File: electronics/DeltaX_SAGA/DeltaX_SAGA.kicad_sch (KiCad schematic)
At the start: 68 parts, among them J1 USB_B_Micro, J10 Motor3_Encoder, J11 Motor1_OUT, J12 Motor2_OUT, J13 Motor3_OUT, J14 TestPt1, J15 TestPt2, J16 TestGND, J18 STLink, J2 Programmer, J3 Servo Signal, J4 Servo Power, J5 Power(6-38V), J6 Thrower Signal, J7 Thrower Power, J8 Motor1_Encoder, J9 Motor2_Encoder, U1 CM1223, U10 DRV8243, U11 DRV8243, U2 NCP164C, U3 STM32G441KB, U4 NCV8730, U5 NCP164C, U6 MAX14930, U7 MAX14930, U8 MAX12930, U9 DRV8243

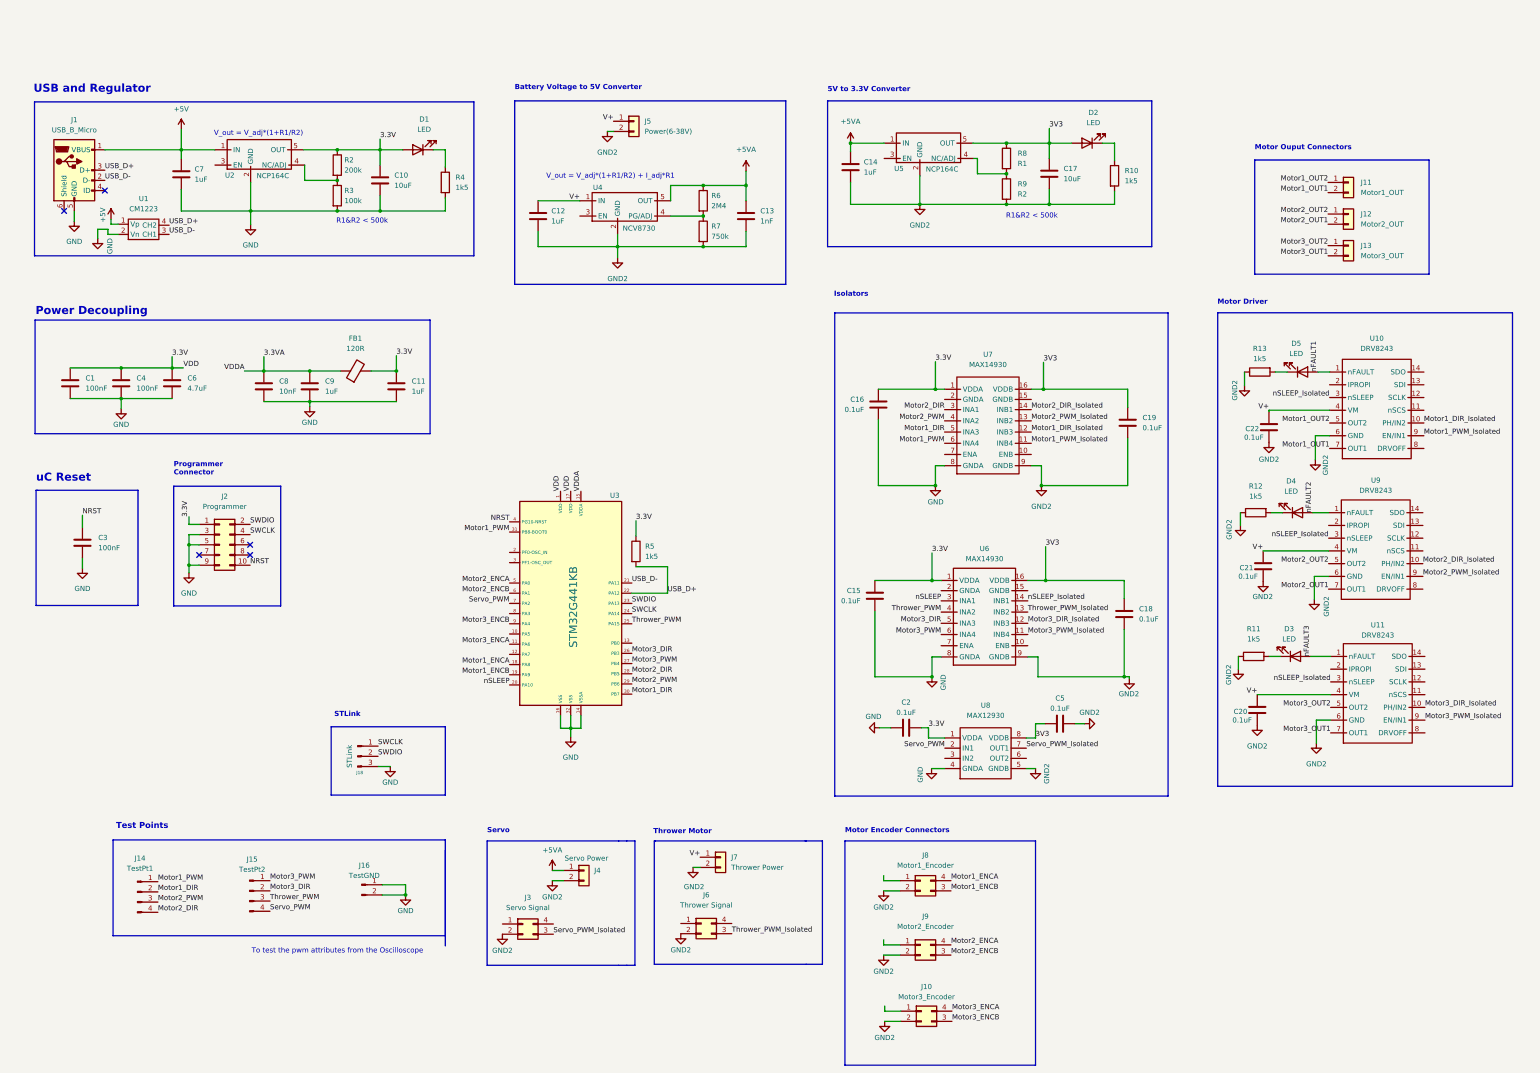
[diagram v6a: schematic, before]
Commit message: Board schematic updated
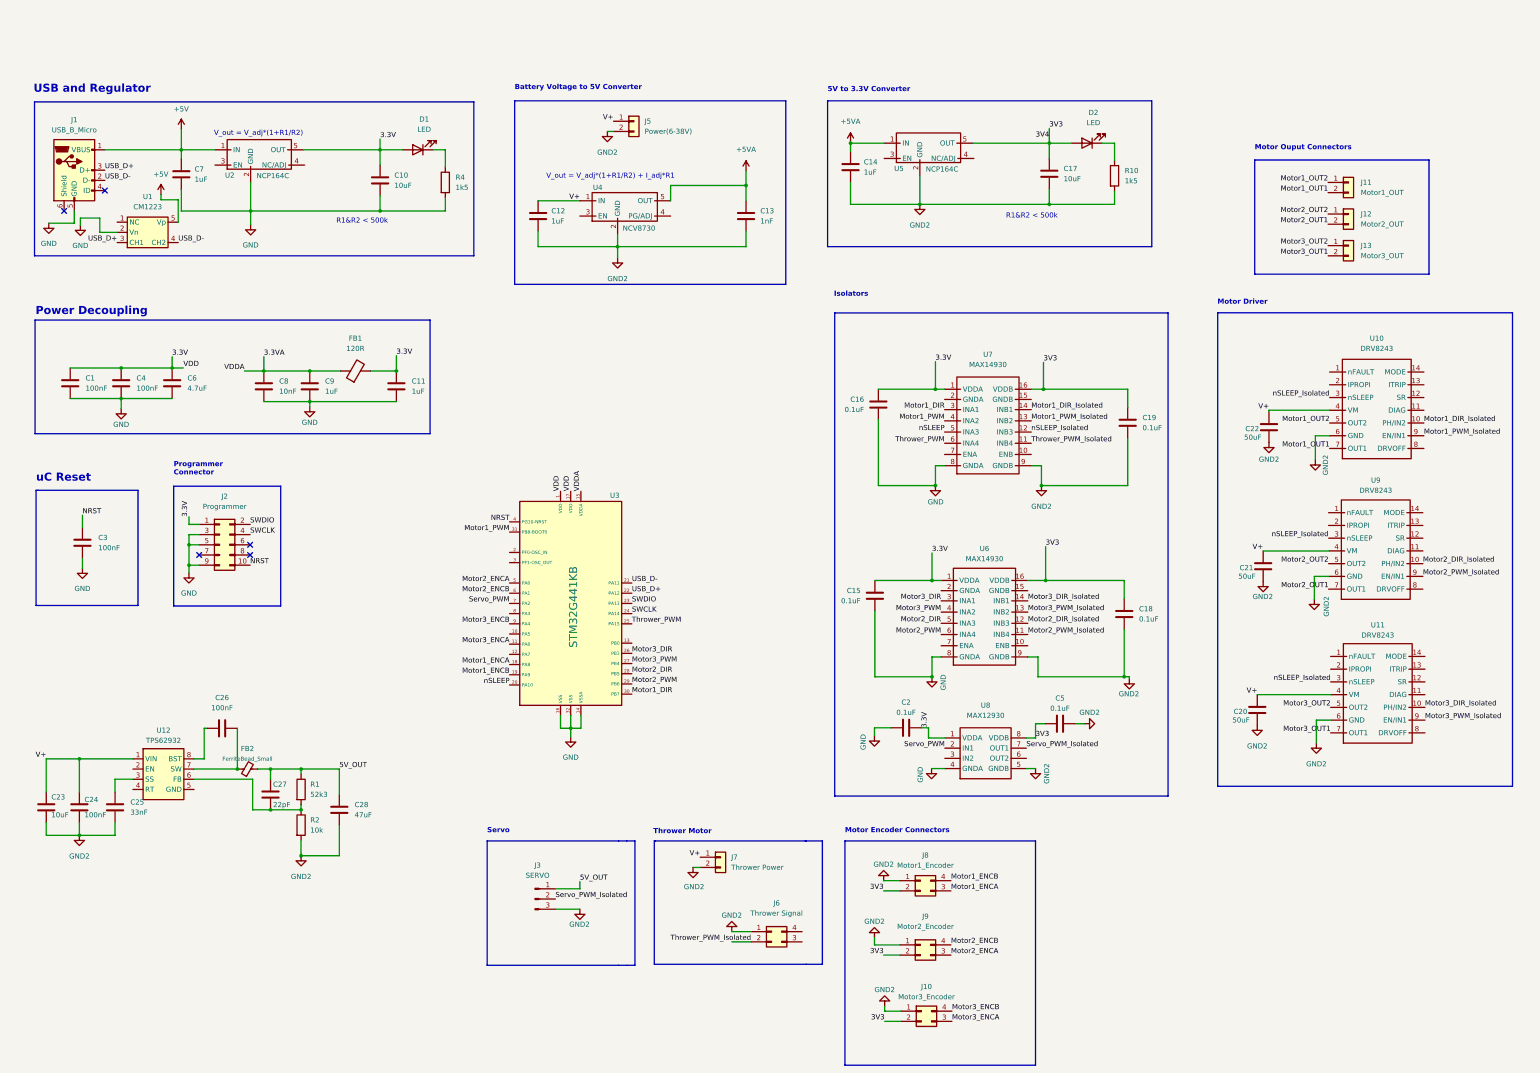
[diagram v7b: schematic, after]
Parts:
- removed D3, D4, D5: LED, LED_SMD:LED_0603_1608Metric, symbol Device:LED
- removed J14: TestPt1, Connector_PinHeader_2.54mm:PinHeader_1x04_P2.54mm_Vertical, symbol Connector:Conn_01x04_Male
- removed J15: TestPt2, Connector_PinHeader_2.54mm:PinHeader_1x04_P2.54mm_Vertical, symbol Connector:Conn_01x04_Male
- removed J16: TestGND, Connector_PinHeader_2.54mm:PinHeader_1x02_P2.54mm_Vertical, symbol Connector:Conn_01x02_Male
- removed J18: STLink, Connector_PinHeader_2.54mm:PinHeader_1x03_P2.54mm_Vertical, symbol Connector:Conn_01x03_Male
- removed J3: Servo Signal, Micro-MaTch215079-4:TE_7-215079-4, symbol Connector_Generic:Conn_02x02_Counter_Clockwise
- removed J4: Servo Power, Connector_PinHeader_2.54mm:PinHeader_1x02_P2.54mm_Vertical_SMD_Pin1Right, symbol Connector_Generic:Conn_01x02
- removed R11, R12, R13, R5: 1k5, Resistor_SMD:R_0402_1005Metric, symbol Device:R
- removed R3: 100k, Resistor_SMD:R_0402_1005Metric, symbol Device:R
- removed R6: 2M4, Resistor_SMD:R_0402_1005Metric, symbol Device:R
- removed R7: 750k, Resistor_SMD:R_0402_1005Metric, symbol Device:R
- removed R8: R1, Resistor_SMD:R_0402_1005Metric, symbol Device:R
- removed R9: R2, Resistor_SMD:R_0402_1005Metric, symbol Device:R
- added C23: 10uF, Capacitor_SMD:C_0603_1608Metric, symbol Device:C
- added C24, C26: 100nF, Capacitor_SMD:C_0603_1608Metric, symbol Device:C
- added C25: 33nF, Capacitor_SMD:C_0603_1608Metric, symbol Device:C
- added C27: 22pF, Capacitor_SMD:C_0603_1608Metric, symbol Device:C
- added C28: 47uF, Capacitor_SMD:C_0603_1608Metric, symbol Device:C
- added FB2: FerriteBead_Small, Inductor_SMD:L_0603_1608Metric, symbol Device:FerriteBead_Small
- added J3: SERVO, Connector_PinHeader_2.54mm:PinHeader_1x03_P2.54mm_Vertical, symbol Connector:Conn_01x03_Male
- added R1: 52k3, Resistor_SMD:R_0603_1608Metric, symbol Device:R
- added U12: TPS62932, TPS62933:TPS62933, symbol TPS62932:TPS62932
- C1, C11, C12, C13, C14, C15, C16, C18, C19, C2, C3, C4, C5, C7, C8, C9: footprint Capacitor_SMD:C_0402_1005Metric -> Capacitor_SMD:C_0603_1608Metric
- C20, C21, C22: value 0.1uF -> 50uF; footprint Capacitor_SMD:C_0402_1005Metric -> Capacitor_SMD:C_0603_1608Metric
- R10, R4: footprint Resistor_SMD:R_0402_1005Metric -> Resistor_SMD:R_0603_1608Metric
- R2: value 200k -> 10k; footprint Resistor_SMD:R_0402_1005Metric -> Resistor_SMD:R_0603_1608Metric
- U1: footprint CM1223:SOT192P237X122-4N -> CM1223-02SO:SOT95P280X145-5N
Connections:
- net +5V: now also U1.5 (Vp); no longer U1.1 (Vp)
- net 3.3V: no longer R2.1
- net 3V3: now also J10.2 (Pin_2), J8.2 (Pin_2), J9.2 (Pin_2)
- net GND2: now also J10.1 (Pin_1), J6.1 (Pin_1), J8.1 (Pin_1), J9.1 (Pin_1), R2.2, C23.2, C24.2, C25.2, C28.2, J3.3 (Pin_3); no longer J10.2 (Pin_2), J6.2 (Pin_2), J8.2 (Pin_2), J9.2 (Pin_2)
- net Motor1_DIR: now also U7.3 (INA1); no longer U7.5 (INA3)
- net Motor1_DIR_Isolated: now also U7.14 (INB1); no longer U7.12 (INB3)
- net Motor1_ENCA: now also J8.3 (Pin_3); no longer J8.4 (Pin_4)
- net Motor1_ENCB: now also J8.4 (Pin_4); no longer J8.3 (Pin_3)
- net Motor1_PWM: now also U7.4 (INA2); no longer U7.6 (INA4)
- net Motor1_PWM_Isolated: now also U7.13 (INB2); no longer U7.11 (INB4)
- net Motor2_DIR: now also U6.5 (INA3); no longer U7.3 (INA1)
- net Motor2_DIR_Isolated: now also U6.12 (INB3); no longer U7.14 (INB1)
- net Motor2_ENCA: now also J9.3 (Pin_3); no longer J9.4 (Pin_4)
- net Motor2_ENCB: now also J9.4 (Pin_4); no longer J9.3 (Pin_3)
- net Motor2_PWM: now also U6.6 (INA4); no longer U7.4 (INA2)
- net Motor2_PWM_Isolated: now also U6.11 (INB4); no longer U7.13 (INB2)
- net Motor3_DIR: now also U6.3 (INA1); no longer U6.5 (INA3)
- net Motor3_DIR_Isolated: now also U6.14 (INB1); no longer U6.12 (INB3)
- net Motor3_ENCA: now also J10.3 (Pin_3); no longer J10.4 (Pin_4)
- net Motor3_ENCB: now also J10.4 (Pin_4); no longer J10.3 (Pin_3)
- net Motor3_PWM: now also U6.4 (INA2); no longer U6.6 (INA4)
- net Motor3_PWM_Isolated: now also U6.13 (INB2); no longer U6.11 (INB4)
- net Servo_PWM_Isolated: now also J3.2 (Pin_2)
- net Thrower_PWM: now also U7.6 (INA4); no longer U6.4 (INA2)
- net Thrower_PWM_Isolated: now also J6.2 (Pin_2), U7.11 (INB4); no longer J6.3 (Pin_3), U6.13 (INB2)
- net USB_D+: now also U1.3 (CH1); no longer U1.4 (CH2)
- net USB_D-: now also U1.4 (CH2); no longer U1.3 (CH1)
- net V+: now also C23.1, C24.1, U12.1 (VIN)
- net nSLEEP: now also U7.5 (INA3); no longer U6.3 (INA1)
- net nSLEEP_Isolated: now also U7.12 (INB3); no longer U6.14 (INB1)
- net at U2.4 (NC/ADJ): no longer R2.2
- net nFAULT1: no longer names the net of U10.1 (nFAULT)
- net nFAULT2: no longer names the net of U9.1 (nFAULT)
- net nFAULT3: no longer names the net of U11.1 (nFAULT)
- new net: C26.1, U12.8 (BST)
- new net: C26.2, FB2.1, U12.7 (SW)
- new net: C25.1, U12.3 (SS)
- new net: C27.2, R1.2, R2.1, U12.6 (FB)
- new net 5V_OUT: C27.1, C28.1, FB2.2, J3.1 (Pin_1), R1.1
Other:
- note removed: "STLink"
- note removed: "Test Points"
- note removed: "To test the pwm attributes from the Oscilloscope"
- moved on the sheet: J6

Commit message: Updated the schematic
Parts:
- removed C28: 47uF, Capacitor_SMD:C_0603_1608Metric, symbol Device:C
- removed D2: LED, LED_SMD:LED_0603_1608Metric, symbol Device:LED
- removed FB2: FerriteBead_Small, Inductor_SMD:L_0603_1608Metric, symbol Device:FerriteBead_Small
- removed U12: TPS62932, TPS62933:TPS62933, symbol TPS62932:TPS62932
- removed U5: NCP164C, NCP164C:SOP95P275X110-5N, symbol NCP164C:NCP164C
- added C29, C30, C31, C32, C33, C34, C35, C36, C37, C38: 10uF, Capacitor_SMD:C_0603_1608Metric, symbol Device:C
- added D3, D4, D5: 1N53xxB, Diode_SMD:D_0603_1608Metric, symbol Diode:1N53xxB
- added L1: 7.6uH, SRP6060FA5R6M:SRP6060FA5R6M, symbol Device:L
- added Q1, Q2, Q3: BUK6Y10, BUK6Y10:TO127P600X120-5N, symbol BUK6Y10:BUK6Y10
- added R11, R12: 3k, Resistor_SMD:R_0603_1608Metric, symbol Device:R
- added R3, R6, R8: 100, Resistor_SMD:R_0603_1608Metric, symbol Device:R
- added R5, R7, R9: 10, Resistor_SMD:R_0603_1608Metric, symbol Device:R
- added U5: TPS62933, TPS62933:TPS62933, symbol TPS62933:TPS62933
- C14: value 1uF -> 10uF
- C20, C21, C22: value 50uF -> 10uF
- C27: value 22pF -> 100uF
- R10: value 1k5 -> 3k
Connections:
- net +5V: now also U2.3 (EN)
- net +5VA: now also C18.2, C19.2, C5.1, U6.16 (VDDB), U7.16 (VDDB), U8.8 (VDDB); no longer C14.1
- net GND: now also J10.1 (Pin_1), J8.1 (Pin_1), J9.1 (Pin_1)
- net GND2: now also C27.1, R10.1, R2.1, U10.11 (DIAG), U10.14 (MODE), U10.8 (DRVOFF), U11.11 (DIAG), U11.14 (MODE), U11.8 (DRVOFF), U9.11 (DIAG), U9.14 (MODE), U9.8 (DRVOFF), C29.2, C30.2, C31.2, C32.2, C33.2, C34.2, C35.2, C36.2, C37.2, C38.2, R11.1, R12.1, R3.2, R5.2, R6.2, R7.2, R8.2, R9.2, U5.4 (GND); no longer J10.1 (Pin_1), J8.1 (Pin_1), J9.1 (Pin_1), R10.2, R2.2
- net Motor1_ENCA: now also U3.5 (PA0); no longer U3.18 (PA8)
- net Motor1_ENCB: now also U3.6 (PA1); no longer U3.19 (PA9)
- net Motor2_ENCA: now also U3.11 (PA6); no longer U3.5 (PA0)
- net Motor2_ENCB: now also U3.9 (PA4); no longer U3.6 (PA1)
- net Motor3_ENCA: now also U3.18 (PA8); no longer U3.11 (PA6)
- net Motor3_ENCB: now also U3.19 (PA9); no longer U3.9 (PA4)
- net V+: now also Q1.5 (D), Q2.5 (D), Q3.5 (D), U5.3 (VIN); no longer C20.1, C21.1, C22.1, U10.4 (VM), U11.4 (VM), U9.4 (VM)
- net at C26.1: now also U5.6 (BST)
- net at C26.2: now also L1.1
- net at C25.1: now also U5.7 (SS)
- net +5VD: now reaches C27.2, R1.2
- net +5VD: now also J3.1 (Pin_1), L1.2; no longer R2.1
- net at U11.2 (IPROPI): now also R12.2
- net at U10.2 (IPROPI): now also R11.2
- net at U9.2 (IPROPI): now also R10.2
- net 3.3V renamed +3.3V
- net +3.3V: now also J10.2 (Pin_2), J8.2 (Pin_2), J9.2 (Pin_2)
- removed net 3V3: C17.1, C18.2, C19.2, C5.1, J10.2 (Pin_2), J8.2 (Pin_2), J9.2 (Pin_2), U6.16 (VDDB), U7.16 (VDDB), U8.8 (VDDB)
- removed net 5V_OUT: C27.1, J3.1 (Pin_1), R1.1
- new net: D5.2 (A), Q3.4 (G), R8.1
- new net: R1.1, R2.2, U5.5 (SW)
- new net: D4.2 (A), Q2.4 (G), R6.1
- new net: D3.2 (A), Q1.4 (G), R3.1
- new net VM: C14.1, C17.1, C20.1, C21.1, C22.1, C29.1, C30.1, C31.1, C32.1, C33.1, C34.1, C35.1, C36.1, C37.1, C38.1, D3.1 (K), D4.1 (K), D5.1 (K), Q1.1 (S), Q1.2, Q1.3, Q2.1 (S), Q2.2, Q2.3, Q3.1 (S), Q3.2, Q3.3, R5.1, R7.1, R9.1, U10.4 (VM), U11.4 (VM), U9.4 (VM)
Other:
- note removed: "5V to 3.3V Converter"
- moved on the sheet: C15, C16, C18, C19, C2, C23, C24, C25, C26, C27, C5, J10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
